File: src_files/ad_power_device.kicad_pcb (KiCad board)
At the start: 2 copper layers, 75 x 75 mm, 508 parts, among them IC1 TPS62867RQYR, IC2 TPS61288RQQR, J1 SPEAKER, J10 Conn_01x02_Male, J11 USB_C_Receptacle, J12 DEBUG_4G, J13 U.FL-R-SMT-1(10), J14 U.FL-R-SMT-1(10), J15 U.FL-R-SMT-1(10), J16 U.FL-R-SMT-1(10), J2 5622-6309-ML, J3 205957-0271, J4 2001-1-2-21-00-BK, J5 3-1734592-0, J6 3-1734592-0, J7 Conn_01x05_Male, J8 2001-1-2-21-00-BK, J9 SIM_Card, Q1 DTC143ZEBTL, Q10 DTC143ZEBTL, Q11 IRFR9024NTRPBF, Q2 DTC143ZEBTL, Q3 2SK3018, Q4 2SK3018, Q5 2SK3018, Q6 DTC143ZEBTL, Q7 DTC143ZEBTL, Q8 DTC143ZEBTL, Q9 DTC143ZEBTL, SW1 PWR_ON, SW2 RESET BTN, SW3 RECOVER BTN, U1 RK3566, U10 ESD5304D-TP, U11 NFC_VS1797SM, U12 MCDP2900, U13 ZLDO1117G12TA, U14 ESD5304D-TP, U15 ESD5304D-TP, U16 ESD5304D-TP, U17 SY6280AAAC, U18 ESD5304D-TP, U19 quesctel_EG91-EX, U2 RK809, U20 ESD5304D-TP, U21 SY6912A, U3 AP6256, U4 LPDDRS_32_IS43LQ32128A-062BLI, U5 TLV62569PDDCR, U6 TLV62569PDDCR, U7 QUECTEL_L70-RL, U8 ESD5304D-TP, U9 ESD5304D-TP, Y1 32.768KHz, Y2 37.4MHz_10PPM, Y3 24MHz/10ppm, Y4 27MHz

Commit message: updated footprint and schematics
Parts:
- removed D2: LED, LED_SMD:LED_0201_0603Metric_Pad0.64x0.40mm_HandSolder
- removed J10: Conn_01x02_Male, Connector_Phoenix_MC:PhoenixContact_MC_1,5_2-G-3.81_1x02_P3.81mm_Horizontal
- removed J12: DEBUG_4G, Connector_PinHeader_2.54mm:PinHeader_1x02_P2.54mm_Vertical
- removed J15: U.FL-R-SMT-1(10), greencharge-footprints:HRS_U.FL-R-SMT-1(10)
- removed Q1, Q2: DTC143ZEBTL, greencharge-footprints:SOTFL50P160X85-3N
- added C284: 10nF, Capacitor_SMD:C_0402_1005Metric, B.Cu at (23.0, 180.8)
- added C285: 10nF, Capacitor_SMD:C_0402_1005Metric, B.Cu at (31.2, 159.4)
- added D26: SMF11A, Diode_SMD:D_SOD-123, B.Cu at (32.6, 166.0)
- added D27: LED_GREEN, LED_SMD:LED_0603_1608Metric, B.Cu at (37.5, 166.4)
- added JP1: Jumper, TestPoint:TestPoint_2Pads_Pitch2.54mm_Drill0.8mm, F.Cu at (24.2, 212.7)
- added Q12: DTC143ZEBTL, greencharge-footprints:SOTFL50P160X85-3N, B.Cu at (25.2, 180.7)
- added R106: 4.7K, Resistor_SMD:R_0402_1005Metric, B.Cu at (34.1, 161.4)
- added R107: 4.7K, Resistor_SMD:R_0402_1005Metric, B.Cu at (31.2, 161.4)
- added R108: 4.7K, Resistor_SMD:R_0402_1005Metric, B.Cu at (34.1, 163.4)
- added R109: 0R, Resistor_SMD:R_0402_1005Metric, B.Cu at (27.6, 181.5)
- added TP18: PWR_IN+, TestPoint:TestPoint_Pad_2.0x2.0mm, B.Cu at (14.7, 205.9)
- added TP19: PWR_IN-, TestPoint:TestPoint_Pad_2.0x2.0mm, B.Cu at (14.7, 210.0)
- added TP20: DBG_RXD, TestPoint:TestPoint_Pad_2.0x2.0mm, F.Cu at (19.3, 150.6)
- added TP21: DBG_RXD, TestPoint:TestPoint_Pad_2.0x2.0mm, F.Cu at (19.9, 145.8)
- C103, C106, C131, C228, C260, C261, C262, C263, C264, C265, C266, C267, C270, C271, C272, C273, C274, C275, C276, C277, C278, C279, C280, C281, C282, C78, C80, C81, C82, D13, D15, IC2, J13, J14, J16, J3, L11, Q10, Q3, Q4, Q5, Q6, R100, R101, R102, R103, R104, R105, R26, R27, R71, R81, TP12, TP13, TP14, TP15, U6: moved to B.Cu
- C149: value 10uF -> 22uF; moved to F.Cu
- C150: value 100nF -> 22uF; moved to F.Cu
- C226, C230: footprint Capacitor_SMD:CP_Elec_5x5.4 -> Capacitor_Tantalum_SMD:CP_EIA-3216-18_Kemet-A
- C251: value 130pF -> 3200pF
- C283: value 100nF -> 22uF
- D1: value LED -> SS56; footprint LED_SMD:LED_0201_0603Metric_Pad0.64x0.40mm_HandSolder -> greencharge-footprints:SMAG; moved to B.Cu
- D20: value LED -> LED_GREEN
- J4: value 2001-1-2-21-00-BK -> 3-1734592-0; footprint digikey-footprints:HDMI_Mini_Female_2001-1-2-21-00-BK -> greencharge-footprints:TE_3-1734592-0
- J8: value 2001-1-2-21-00-BK -> 3-1734592-0; footprint digikey-footprints:HDMI_Mini_Female_2001-1-2-21-00-BK -> greencharge-footprints:TE_3-1734592-0; moved to B.Cu
- J9: value SIM_Card -> SIM_Card_Shielded; footprint greencharge-footprints:MOLEX_78800-0001 -> greencharge-footprints:GCT_SIM8066-6-1-14-01-A_REVA
- R28: value 0R -> 100K
- R29: value 1K -> 806K
- R30: value 1K -> 91K
- U1: footprint greencharge-footprints:BGA828C65P31X31_2100X2100X161N -> greencharge-footprints:RK366_BGA-565_20x18_15.5x14.4mm
- U13: moved to F.Cu
- U19: value quesctel_EG91-EX -> EG25G; footprint greencharge-footprints:XCVR_EG91EFB-512-SNND -> greencharge-footprints:XCVR_EG25G
- U4: value LPDDRS_32_IS43LQ32128A-062BLI -> LPDDR4_32_IS43LQ32128A-062BLI
- U7: value QUECTEL_L70-RL -> TPS63802DLAR; footprint greencharge-footprints:QUECTEL_L70-R -> greencharge-footprints:VREG_TPS63802DLAR; moved to B.Cu
- moved R104 114.5 mm to (53.3, 217.8)
- moved U6 111.9 mm to (49.4, 216.5)
- moved R103 110.6 mm to (53.3, 215.8)
- moved IC2 110.5 mm to (43.7, 215.8)
- moved C271 106.6 mm to (54.4, 213.8)
- moved R101 106.0 mm to (51.3, 213.9)
- moved C283 95.9 mm to (83.7, 197.4)
- moved R28 94.9 mm to (83.4, 195.7)
- moved TP13 90.1 mm to (41.3, 199.0)
- moved C273 85.0 mm to (43.2, 196.5)
- moved R100 85.0 mm to (40.3, 196.5)
- moved R26 83.4 mm to (83.8, 211.6), turned to 90 degrees
- moved C103 82.3 mm to (85.9, 211.0)
- moved C265 82.0 mm to (85.8, 212.4)
- moved C267 81.8 mm to (82.5, 211.8), turned to 90 degrees
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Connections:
- C149 pad 1: +3V3 -> VBAT
- C150 pad 1: +3V3 -> Net-(C150-Pad1)
- C234 pad 1: /4G_MODULE/USM1_DATA -> Net-(C234-Pad1)
- C283 pad 1: +3V3 -> Net-(C150-Pad1)
- D1 pad 1: Net-(D1-Pad1) -> +5V
- D1 pad 2: +3V3 -> Net-(C150-Pad1)
- J2 pad S2: (no net) -> /SATA1_TX+
- J4 pad 1: /RK3566_PART_C/HDMI_TX2P_PORT+ -> (no net)
- J4 pad 10: /RK3566_PART_C/HDMI_TXCLKP_PORT+ -> (no net)
- J4 pad 11: GND -> (no net)
- J4 pad 12: /RK3566_PART_C/HDMI_TXCLKN_PORT- -> (no net)
- J4 pad 13: /RK3566_PART_C/HDMI_TX_CEC_PORT -> (no net)
- J4 pad 15: /RK3566_PART_C/HDMI_TXDDC_SCL_PORT -> (no net)
- J4 pad 16: /RK3566_PART_C/HDMI_TXDDC_SDA_PORT -> (no net)
- J4 pad 17: GND -> (no net)
- J4 pad 18: /RK3566_PART_C/VCC5V_HDMI_TX -> (no net)
- J4 pad 19: /RK3566_PART_C/HDMI_TX_HPD_PORT -> (no net)
- J4 pad 2: GND -> (no net)
- J4 pad 3: /RK3566_PART_C/HDMI_TX2N_PORT- -> (no net)
- J4 pad 4: /RK3566_PART_C/HDMI_TX1P_PORT+ -> (no net)
- J4 pad 5: GND -> (no net)
- J4 pad 6: /RK3566_PART_C/HDMI_TX1N_PORT- -> (no net)
- J4 pad 7: /RK3566_PART_C/HDMI_TX0P_PORT+ -> (no net)
- J4 pad 8: GND -> (no net)
- J4 pad 9: /RK3566_PART_C/HDMI_TX0N_PORT- -> (no net)
- J5 pad 10: (no net) -> /TP_INT_GPIO0_A5
- J5 pad 13: (no net) -> /LCD_RST_L_GPIO0_C2
- J5 pad 16: (no net) -> /RK3566_PART_C/MIPI_DSI_TX0_D0P+
- J5 pad 17: (no net) -> /RK3566_PART_C/MIPI_DSI_TX0_D0N-
- J5 pad 19: (no net) -> /RK3566_PART_C/MIPI_DSI_TX0_D1P+
- J5 pad 20: (no net) -> /RK3566_PART_C/MIPI_DSI_TX0_D1N-
- J5 pad 25: (no net) -> /RK3566_PART_C/MIPI_DSI_TX0_D2P+
- J5 pad 26: (no net) -> /RK3566_PART_C/MIPI_DSI_TX0_D2N-
- J5 pad 29: (no net) -> /RK3566_PART_C/MIPI_DSI_TX0_D3N-
- J6 pad 10: (no net) -> /TP_INT_GPIO1_B6_DISPLAY_ONE
- J6 pad 12: (no net) -> /RK3566_PART_C/LCD_BL_PWM12_M0_DISPLAY_ONE
- J6 pad 13: (no net) -> /LCD_RST_L_GPIO1_C0_DISPLAY_ONE
- J6 pad 16: (no net) -> /RK3566_PART_C/MIPI_DSI_TX1_D0P+
- J6 pad 17: (no net) -> /RK3566_PART_C/MIPI_DSI_TX1_D0N-
- J6 pad 20: (no net) -> /RK3566_PART_C/MIPI_DSI_TX1_D1N-
- J6 pad 25: (no net) -> /RK3566_PART_C/MIPI_DSI_TX1_D2P+
- J6 pad 26: (no net) -> /RK3566_PART_C/MIPI_DSI_TX1_D2N-
- J6 pad 29: (no net) -> /RK3566_PART_C/MIPI_DSI_TX1_D3N-
- J6 pad 5: (no net) -> /GPIO1_B4_DISPLAY_ONE
- J8 pad 1: /RK3566_PART_C/DP TO HDMI/TMDS_D2+ -> (no net)
- J8 pad 10: /RK3566_PART_C/DP TO HDMI/TMDS_CLK+ -> (no net)
- J8 pad 11: GND -> (no net)
- J8 pad 12: /RK3566_PART_C/DP TO HDMI/TMDS_CLK- -> (no net)
- J8 pad 13: /RK3566_PART_C/DP TO HDMI/CEC -> (no net)
- J8 pad 15: /RK3566_PART_C/DP TO HDMI/DDC_CLK -> (no net)
- J8 pad 16: /RK3566_PART_C/DP TO HDMI/DDC_DATA -> (no net)
- J8 pad 17: GND -> (no net)
- J8 pad 18: /RK3566_PART_C/DP TO HDMI/VCC5V_HDMI_TX -> (no net)
- J8 pad 19: /RK3566_PART_C/DP TO HDMI/HPD -> (no net)
- J8 pad 2: GND -> (no net)
- J8 pad 3: /RK3566_PART_C/DP TO HDMI/TMDS_D2- -> (no net)
- J8 pad 4: /RK3566_PART_C/DP TO HDMI/TMDS_D1+ -> (no net)
- J8 pad 5: GND -> (no net)
- J8 pad 6: /RK3566_PART_C/DP TO HDMI/TMDS_D1- -> (no net)
- J8 pad 7: /RK3566_PART_C/DP TO HDMI/TMDS_D0+ -> (no net)
- J8 pad 8: GND -> (no net)
- J8 pad 9: /RK3566_PART_C/DP TO HDMI/TMDS_D0- -> (no net)
- Q10 pad 1: Net-(Q10-Pad1) -> /4G_MODULE/Status_indicator
- Q8 pad 1: (no net) -> /4G_MODEM_ON
- Q8 pad 3: Net-(Q8-Pad3) -> /4G_MODULE/PWR_EN
- Q9 pad 1: (no net) -> /4G_MODEM_RESETn
- Q9 pad 3: Net-(Q9-Pad3) -> /4G_MODULE/RESET_n
- R17 pad 1: (no net) -> /I2S2_SCLK_TX_M0
- R18 pad 1: (no net) -> /I2S2_SDI_M0
- R28 pad 1: Net-(J15-Pad2) -> Net-(C150-Pad1)
- R29 pad 1: Net-(D1-Pad1) -> Net-(C150-Pad1)
- R29 pad 2: Net-(Q1-Pad3) -> /BATTERY_CHARGER/FB
- R30 pad 1: Net-(D2-Pad1) -> /BATTERY_CHARGER/FB
- R30 pad 2: Net-(Q2-Pad3) -> GND
- R37 pad 1: (no net) -> Net-(R37-Pad1)
- R38 pad 1: (no net) -> Net-(R38-Pad1)
- R40 pad 1: (no net) -> Net-(R40-Pad1)
- R41 pad 1: (no net) -> Net-(R41-Pad1)
- R41 pad 2: /RK3566_PART_C/HDMI_TX0P_PORT+ -> (no net)
- R42 pad 1: (no net) -> Net-(R42-Pad1)
- R43 pad 1: (no net) -> Net-(R43-Pad1)
- R44 pad 1: (no net) -> Net-(R44-Pad1)
- R48 pad 2: (no net) -> /RK3566_LPDDR3/I2C1_SCL
- R49 pad 2: (no net) -> /RK3566_LPDDR3/I2C1_SDA
- R79 pad 2: Net-(R79-Pad2) -> /4G_MODULE/ANT_GNSS_GPS
- R80 pad 2: Net-(R80-Pad2) -> /4G_MODULE/ANT_MAIN
- R81 pad 1: /4G_MODULE/USM1_DATA -> Net-(C234-Pad1)
- TP9 pad 1: (no net) -> Net-(TP9-Pad1)
- U1 pad V1: (no net) -> Net-(U1-PadV1)
- U1 pad V2: (no net) -> Net-(U1-PadV2)
- U12 pad A3: (no net) -> /RK3566_PART_C/EDP_TX_D2-
- U12 pad A4: (no net) -> /RK3566_PART_C/EDP_TX_D2+
- U12 pad A5: (no net) -> /RK3566_PART_C/EDP_TX_D1-
- U12 pad A6: (no net) -> /RK3566_PART_C/EDP_TX_D1+
- U12 pad A8: (no net) -> /RK3566_PART_C/EDP_TX_D0+
- U12 pad F6: (no net) -> /RK3566_PART_C/MCDP_I2C_SCL
- U19 pad 10: /4G_MODULE_USB_D- -> /4G_MODULE/USM_GND
- U19 pad 11: (no net) -> /4G_MODULE/DBG_RXD
- U19 pad 12: (no net) -> /4G_MODULE/DBG_TXD
- U19 pad 14: (no net) -> /4G_MODULE/USM1_VDD
- U19 pad 15: Net-(Q8-Pad3) -> /4G_MODULE/USM1_DATA
- U19 pad 16: (no net) -> /4G_MODULE/USM1_CLK
- U19 pad 17: Net-(Q9-Pad3) -> /4G_MODULE/USM1_RST
- U19 pad 18: (no net) -> Net-(U19-Pad113)
- U19 pad 19: (no net) -> GND
- U19 pad 2: (no net) -> /AP_READY
- U19 pad 20: (no net) -> /4G_MODULE/RESET_n
- U19 pad 21: Net-(Q10-Pad1) -> /4G_MODULE/PWR_EN
- U19 pad 22: Net-(J12-Pad2) -> GND
- U19 pad 23: Net-(J12-Pad1) -> (no net)
- U19 pad 3: GND -> Net-(U19-Pad113)
- U19 pad 31: GND -> (no net)
- U19 pad 32: VCC_3V3 -> (no net)
- U19 pad 33: VCC_3V3 -> (no net)
- U19 pad 36: (no net) -> GND
- U19 pad 41: (no net) -> /4G_MODULE_SDA
- U19 pad 42: (no net) -> /4G_MODULE_SCL
- U19 pad 43: /4G_MODULE/USM1_VDD -> Net-(U19-Pad113)
- U19 pad 44: /4G_MODULE/USM1_RST -> (no net)
- U19 pad 45: /4G_MODULE/USM1_DATA -> (no net)
- U19 pad 46: /4G_MODULE/USM1_CLK -> GND
- U19 pad 47: /4G_MODULE/USM_GND -> /4G_MODULE/ANT_GNSS_GPS
- U19 pad 49: (no net) -> /4G_MODULE/ANT_MAIN
- U19 pad 51: (no net) -> GND
- U19 pad 52: VCC_3V3 -> GND
- U19 pad 53: VCC_3V3 -> GND
- U19 pad 55: GND -> Net-(U19-Pad113)
- U19 pad 56: Net-(R79-Pad2) -> GND
- U19 pad 57: (no net) -> VCC_3V3
- U19 pad 58: GND -> VCC_3V3
- U19 pad 59: GND -> VCC_3V3
- U19 pad 6: (no net) -> /4G_MODULE/Net_status
- U19 pad 60: Net-(R80-Pad2) -> VCC_3V3
- U19 pad 61: GND -> /4G_MODULE/Status_indicator
- U19 pad 62: GND -> (no net)
- U19 pad 67: GND -> (no net)
- U19 pad 68: GND -> (no net)
- U19 pad 69: GND -> /4G_MODULE_USB_D+
- U19 pad 7: (no net) -> /4G_MODULE/1.8V_local_ldo
- U19 pad 70: GND -> /4G_MODULE_USB_D-
- U19 pad 71: GND -> VCC_3V3
- U19 pad 8: VCC_3V3 -> GND
- U19 pad 85: (no net) -> GND
- U19 pad 86: (no net) -> GND
- U19 pad 87: (no net) -> GND
- U19 pad 88: (no net) -> GND
- U19 pad 9: /4G_MODULE_USB_D+ -> GND
- U19 pad 92: (no net) -> GND
- U19 pad 93: (no net) -> GND
- U19 pad 94: (no net) -> GND
- U19 pad 95: (no net) -> GND
- U19 pad 96: (no net) -> GND
- U19 pad 97: (no net) -> GND
- U19 pad 98: (no net) -> GND
- U19 pad 99: (no net) -> GND
- U2 pad 16: /I2S1_MCLK_M0_RK809 -> (no net)
- U3 pad 13: (no net) -> /WIFI_WAKE_HOST_H_GPIO2_B2
- U3 pad 16: (no net) -> /SDMMC1_CLK
- U3 pad 17: (no net) -> /SDMMC1_CMD
- U3 pad 37: (no net) -> /BT_WAKE_HOST_H_GPIO2_C0
- U3 pad 41: (no net) -> /UART1_CTSn_M0
- U3 pad 42: (no net) -> /UART1_TX_M0
- U3 pad 44: (no net) -> /UART1_RTSn_M0
- U7 pad 1: GND -> VBAT
- U7 pad 10: GND -> VBAT
- U7 pad 2: (no net) -> GND
- U7 pad 3: (no net) -> GND
- U7 pad 4: /IPPS -> /BATTERY_CHARGER/FB
- U7 pad 5: /STANDBY -> Net-(R28-Pad2)
- U7 pad 6: (no net) -> Net-(C150-Pad1)
- U7 pad 8: +3V3 -> GND
- U7 pad 9: +3V3 -> (no net)
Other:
- board text added: "4G_MODULE + GPS MODULE"
- board text added: "5G_RADAR_MODULE"
- board text added: "ANTENNA"
- board text added: "AP6256_WIFI/BT"
- board text added: "AUDIO_OUT"
- board text added: "BAT_CHARGER_IC"
- board text added: "HDMI_MINI"
- board text added: "MIPI_CON_1"
- board text added: "MIPI_CON_2"
- board text added: "MIPI_CON_3"
- board text added: "MIPI_CON_4"
- board text added: "NANO_SIM_CON"
- board text added: "NFC_READER"
- board text added: "RAM_LPDDR4_4GB"
- board text added: "RK3566_MAIN_IC"
- board text added: "RK809_PMIC"
- board text added: "SATA_CONNECTOR"
- board text added: "USB_PWR IN_OTG"
- board text added: "VS1797SM"

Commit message: complete update on schematiC + FOOTPRINT
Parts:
- removed D10, D4, D5: 1N5819WS, Diode_SMD:D_SOD-323
- removed D11, D6: ESD5451R-2/TR, greencharge-footprints:DFP1006-2L
- removed D7, D8, D9: D, Diode_SMD:D_SOD-123
- removed FB3, FB4: MPZ1608S471ATD25, Inductor_SMD:L_0603_1608Metric
- removed Q3, Q4, Q5: 2SK3018, digikey-footprints:SOT-23-3
- removed R66: 100K, Resistor_SMD:R_0805_2012Metric
- removed R67: 249OHM/1%, Resistor_SMD:R_0603_1608Metric
- removed R68, R69, R70: 4.7K, Resistor_SMD:R_0402_1005Metric
- removed U13: ZLDO1117G12TA, Package_TO_SOT_SMD:SOT-223-3_TabPin2
- removed U14, U15, U16: ESD5304D-TP, greencharge-footprints:ESD5304D-TP
- added C286: 100nF, Capacitor_SMD:C_0402_1005Metric, F.Cu at (22.6, 193.8)
- added C287: 100nF, Capacitor_SMD:C_0402_1005Metric, F.Cu at (56.7, 159.0)
- added C288: 100nF, Capacitor_SMD:C_0402_1005Metric, F.Cu at (59.6, 159.0)
- added C289: 100nF, Capacitor_SMD:C_0402_1005Metric, F.Cu at (81.4, 169.8)
- added C290: 100nF, Capacitor_SMD:C_0402_1005Metric, F.Cu at (81.1, 168.2)
- added C291: 100nF, Capacitor_SMD:C_0402_1005Metric, F.Cu at (39.0, 156.3)
- added C292: 100nF, Capacitor_SMD:C_0402_1005Metric, F.Cu at (59.6, 157.0)
- added C293: 100nF, Capacitor_SMD:C_0402_1005Metric, F.Cu at (69.9, 161.4)
- added C294: 100nF, Capacitor_SMD:C_0402_1005Metric, F.Cu at (81.0, 172.7)
- added C295: 1uF, Capacitor_SMD:C_0402_1005Metric, F.Cu at (80.9, 171.3)
- added C296: 1uF, Capacitor_SMD:C_0402_1005Metric, F.Cu at (62.4, 159.0)
- added C297: 100nF, Capacitor_SMD:C_0402_1005Metric, F.Cu at (27.2, 185.3)
- added D2: 1N5819WS, Diode_SMD:D_SOD-323, F.Cu at (31.6, 186.1)
- added L15: 470nH, greencharge-footprints:FNR4018SR47NT, B.Cu at (27.4, 203.7)
- added Y5: ASE-27.000MHZ-LR-T(27MHz), Crystal:Crystal_SMD_EuroQuartz_MT-4Pin_3.2x2.5mm, F.Cu at (35.9, 195.8)
- C176, C191, C203, C205: moved to F.Cu
- C190, C208: value 1uF -> 100nF; moved to F.Cu
- C192, C193, C196, C197, C199, C200, C201, C202: value 0.1uF -> 100nF; moved to F.Cu
- C194: value 22pF -> 100nF
- C195: value 22pF -> 100nF; moved to F.Cu
- C198: value 0.1uf -> 100nF; moved to F.Cu
- C204: value 2.2uF -> 10uF; footprint Capacitor_SMD:C_0402_1005Metric -> Capacitor_SMD:C_0603_1608Metric; moved to F.Cu
- C206: value 10uF -> 1uF; footprint Capacitor_SMD:C_0603_1608Metric -> Capacitor_SMD:C_0402_1005Metric
- C207: value 1uF -> 0.1uF; moved to F.Cu
- D3: value 1N5819WS -> ESD5451R-2/TR; footprint Diode_SMD:D_SOD-323 -> greencharge-footprints:DFP1006-2L
- J9: value SIM_Card_Shielded -> SIM8066-6-1-14-01-A_REVA
- R46: value 1K -> 2.2K_5%; moved to F.Cu
- R47: value 100K -> 2.2K_402; moved to F.Cu
- R60: value 10K -> 2.2K_5%
- R61: value 10K -> 2.2K_402; moved to F.Cu
- R62: value 27K -> 1K
- R63: value 1.8K -> 2.2K_402; moved to F.Cu
- R64: value 1.8K -> 1K; moved to F.Cu
- R65: value 2.2K_402 -> 1KK; moved to F.Cu
- U10: value ESD5304D-TP -> TC358860XBG; footprint greencharge-footprints:ESD5304D-TP -> greencharge-footprints:TC358860XBG
- U12: value MCDP2900 -> TLV71211DBVR; footprint greencharge-footprints:BGA-64_8x8_7.0x7.0mm_MCDP2900 -> Package_TO_SOT_SMD:SOT-23-5; moved to F.Cu
- U8: value ESD5304D-TP -> TC358779XBG; footprint greencharge-footprints:ESD5304D-TP -> greencharge-footprints:TC358779XBG
- U9: value ESD5304D-TP -> ZLDO1117G12TA; footprint greencharge-footprints:ESD5304D-TP -> Package_TO_SOT_SMD:SOT-223-3_TabPin2
- Y4: value 27MHz -> ASE-27.000MHZ-LR-T(27MHz); footprint Crystal:Crystal_SMD_2016-4Pin_2.0x1.6mm -> Crystal:Crystal_SMD_EuroQuartz_MT-4Pin_3.2x2.5mm
- moved C206 63.7 mm to (69.9, 159.4)
- moved R61 61.5 mm to (19.8, 186.7)
- moved C208 57.1 mm to (56.7, 157.0), turned to 0 degrees
- moved R64 52.8 mm to (26.6, 190.5)
- moved C195 51.4 mm to (62.5, 172.6), turned to 0 degrees
- moved R62 50.8 mm to (22.6, 191.8)
- moved R63 48.7 mm to (86.0, 169.2)
- moved R47 48.5 mm to (60.8, 170.6)
- moved C176 45.9 mm to (28.4, 186.6)
- moved C196 45.2 mm to (59.6, 175.1), turned to 0 degrees
- moved U12 45.1 mm to (65.9, 160.2), turned to 0 degrees
- moved C201 42.8 mm to (59.6, 173.1), turned to 0 degrees
- moved C202 41.8 mm to (56.7, 175.1), turned to 0 degrees
- moved C205 40.7 mm to (57.3, 170.8), turned to 0 degrees
- moved R60 40.6 mm to (29.5, 189.5)
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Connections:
- net /RK3566_PART_C/MIPI_DSI_TX1_D0N- renamed /RK3566_PART_C/MIPI_DSI_TX1_D0-
- net /RK3566_PART_C/MIPI_DSI_TX1_D0P+ renamed /RK3566_PART_C/MIPI_DSI_TX1_D0+
- net /RK3566_PART_C/MIPI_DSI_TX1_D1N- renamed /RK3566_PART_C/MIPI_DSI_TX1_D1-
- net /RK3566_PART_C/MIPI_DSI_TX1_D2N- renamed /RK3566_PART_C/MIPI_DSI_TX1_D2-
- net /RK3566_PART_C/MIPI_DSI_TX1_D2P+ renamed /RK3566_PART_C/MIPI_DSI_TX1_D2+
- net /RK3566_PART_C/MIPI_DSI_TX1_D3N- renamed /RK3566_PART_C/MIPI_DSI_TX1_D3-
- C176 pad 1: /RK3566_PART_C/VCC5V_HDMI_TX -> +3V3
- C190 pad 1: +5V -> VCC_3V3
- C191 pad 1: /RK3566_PART_C/DP TO HDMI/1.2v_FB -> Net-(C191-Pad1)
- C193 pad 1: Net-(C193-Pad1) -> +3V3
- C194 pad 1: /RK3566_PART_C/DP TO HDMI/1.2v_FB -> +1V2
- C194 pad 2: /RK3566_PART_C/DP TO HDMI/TCLK -> GND
- C195 pad 1: /RK3566_PART_C/DP TO HDMI/1.2v_FB -> +1V2
- C195 pad 2: /RK3566_PART_C/DP TO HDMI/XTAL -> GND
- C196 pad 1: +3V3 -> +1V2
- C198 pad 1: GND -> +3V3
- C198 pad 2: /RK3566_PART_C/DP TO HDMI/1.2v_FB -> GND
- C199 pad 1: Net-(C199-Pad1) -> +1V2
- C200 pad 1: Net-(C199-Pad1) -> +1V2
- C201 pad 1: /RK3566_PART_C/DP TO HDMI/1.2v_FB -> +1V2
- C202 pad 1: GND -> +1V2
- C202 pad 2: +1V2 -> GND
- C203 pad 1: /RK3566_PART_C/DP TO HDMI/1.2v_FB -> Net-(C203-Pad1)
- C204 pad 1: Net-(C204-Pad1) -> +3V3
- C205 pad 1: +3V3 -> +1V2
- C206 pad 1: +1V2 -> +3V3
- C207 pad 1: +5V -> Net-(C207-Pad1)
- C208 pad 1: /RK3566_PART_C/DP TO HDMI/VCC5V_HDMI_TX -> +1V1
- C236 pad 1: /4G_MODULE/USM_GND -> GND
- D3 pad 1: Net-(D3-Pad1) -> /RK3566_PART_C/VCC5V_HDMI_TX
- D3 pad 2: +5V -> GND
- J4 pad 1: (no net) -> +5V
- J4 pad 10: (no net) -> /TP_INT_GPIO0_A5_DISPLAY_TWO
- J4 pad 11: (no net) -> /BL_EN_GPIO0_C0_DISPLAY_TWO
- J4 pad 15: (no net) -> GND
- J4 pad 16: (no net) -> /RK3566_PART_C/MIPI_D0+
- J4 pad 17: (no net) -> /RK3566_PART_C/MIPI_D0-
- J4 pad 18: (no net) -> GND
- J4 pad 19: (no net) -> /RK3566_PART_C/MIPI_D1+
- J4 pad 2: (no net) -> +5V
- J4 pad 20: (no net) -> /RK3566_PART_C/MIPI_D1-
- J4 pad 21: (no net) -> GND
- J4 pad 22: (no net) -> /RK3566_PART_C/MIPI_C+
- J4 pad 23: (no net) -> /RK3566_PART_C/MIPI_C-
- J4 pad 24: (no net) -> GND
- J4 pad 25: (no net) -> /RK3566_PART_C/MIPI_D2+
- J4 pad 26: (no net) -> /RK3566_PART_C/MIPI_D2-
- J4 pad 27: (no net) -> GND
- J4 pad 28: (no net) -> /RK3566_PART_C/MIPI_D3+
- J4 pad 29: (no net) -> /RK3566_PART_C/MIPI_D3-
- J4 pad 3: (no net) -> +5V
- J4 pad 30: (no net) -> GND
- J4 pad 4: (no net) -> GND
- J4 pad 5: (no net) -> /GPIO1_C2_u_DISPLAY_TWO
- J4 pad 6: (no net) -> VCC3V3_EXT
- J4 pad 7: (no net) -> /I2C2_SDA_M0_TP
- J4 pad 8: (no net) -> /I2C2_SCL_M0_TP
- J4 pad S1: Net-(J4-PadS1) -> GND
- J4 pad S2: Net-(J4-PadS1) -> GND
- J8 pad 1: (no net) -> +5V
- J8 pad 10: (no net) -> /RK3566_PART_C/TP_INT_GPIO0_A5_DISPLAY_THREE
- J8 pad 11: (no net) -> /RK3566_PART_C/BL_EN_GPIO0_C0_DISPLAY_THREE
- J8 pad 15: (no net) -> GND
- J8 pad 16: (no net) -> /RK3566_PART_C/DP TO MIPI/DSIODP_MIPI_D0+
- J8 pad 17: (no net) -> /RK3566_PART_C/DP TO MIPI/DSIODM_MIPI_D0-
- J8 pad 18: (no net) -> GND
- J8 pad 19: (no net) -> /RK3566_PART_C/DP TO MIPI/DSIODP_MIPI_D1+
- J8 pad 2: (no net) -> +5V
- J8 pad 20: (no net) -> /RK3566_PART_C/DP TO MIPI/DSIODM_MIPI_D1-
- J8 pad 21: (no net) -> GND
- J8 pad 22: (no net) -> /RK3566_PART_C/DP TO MIPI/DSIODP_MIPI_C+
- J8 pad 23: (no net) -> /RK3566_PART_C/DP TO MIPI/DSIODM_MIPI_C-
- J8 pad 24: (no net) -> GND
- J8 pad 25: (no net) -> /RK3566_PART_C/DP TO MIPI/DSIODP_MIPI_D2+
- J8 pad 26: (no net) -> /RK3566_PART_C/DP TO MIPI/DSIODM_MIPI_D2-
- J8 pad 27: (no net) -> GND
- J8 pad 28: (no net) -> /RK3566_PART_C/DP TO MIPI/DSIODP_MIPI_D3+
- J8 pad 29: (no net) -> /RK3566_PART_C/DP TO MIPI/DSIODM_MIPI_D3-
- J8 pad 3: (no net) -> +5V
- J8 pad 30: (no net) -> GND
- J8 pad 4: (no net) -> GND
- J8 pad 5: (no net) -> /RK3566_PART_C/GPIO1_C2_u_DISPLAY_THREE
- J8 pad 6: (no net) -> VCC3V3_EXT
- J8 pad 7: (no net) -> /I2C2_SDA_M0_TP
- J8 pad 8: (no net) -> /I2C2_SCL_M0_TP
- J8 pad 9: (no net) -> /RK3566_PART_C/LCD_3_ENGPIO1_C3_u_TO_DISPLAY
- J8 pad S1: Net-(J8-PadS1) -> GND
- J8 pad S2: Net-(J8-PadS1) -> GND
- J9 pad C1: (no net) -> /4G_MODULE/USM1_VDD
- J9 pad C2: (no net) -> Net-(C237-Pad1)
- J9 pad C3: (no net) -> Net-(C235-Pad1)
- J9 pad C5: (no net) -> GND
- J9 pad C7: (no net) -> Net-(C234-Pad1)
- J9 pad CD: (no net) -> GND
- J9 pad G1: (no net) -> GND
- J9 pad G2: (no net) -> GND
- J9 pad G3: (no net) -> GND
- J9 pad G4: (no net) -> GND
- R41 pad 2: (no net) -> /RK3566_PART_C/HDMI_TX0P_PORT+
- R46 pad 1: /RK3566_PART_C/HDMI_TX_HPDIN -> VCC3V3_PMU
- R46 pad 2: /RK3566_PART_C/HDMI_TX_HPD_PORT -> /RK3566_PART_C/MCDP_I2C_SDA
- R47 pad 1: /RK3566_PART_C/HDMI_TX_HPD_PORT -> +3V3
- R47 pad 2: GND -> Net-(C191-Pad1)
- R60 pad 1: VCC_3V3 -> VCC3V3_PMU
- R60 pad 2: /HDMITX_SDA -> /RK3566_PART_C/MCDP_I2C_SCL
- R61 pad 1: VCC_3V3 -> +3V3
- R61 pad 2: /HDMITX_SCL -> Net-(C203-Pad1)
- R62 pad 1: VCC_3V3 -> +1V1
- R62 pad 2: /HDMITX_CEC_M0 -> Net-(R62-Pad2)
- R63 pad 1: Net-(D3-Pad1) -> +3V3
- R63 pad 2: /RK3566_PART_C/HDMI_TXDDC_SCL_PORT -> Net-(C207-Pad1)
- R64 pad 1: Net-(D4-Pad1) -> Net-(R64-Pad1)
- R64 pad 2: /RK3566_PART_C/HDMI_TXDDC_SDA_PORT -> /RK3566_PART_C/HDMI_TX_HPDIN
- R65 pad 1: +3V3 -> Net-(R64-Pad1)
- R65 pad 2: Net-(C193-Pad1) -> GND
- R71 pad 1: (no net) -> /RK3566_LPDDR3/UART2_TX_M0_DEBUG
- U1 pad A27: (no net) -> /TP_INT_GPIO0_A5_DISPLAY_TWO
- U1 pad A29: (no net) -> /BL_EN_GPIO0_C0_DISPLAY_TWO
- U1 pad AP3: (no net) -> /RK3566_PART_C/BL_EN_GPIO0_C0_DISPLAY_THREE
- U1 pad AP4: (no net) -> /RK3566_PART_C/TP_INT_GPIO0_A5_DISPLAY_THREE
- U1 pad AP9: (no net) -> /RK3566_PART_C/GPIO1_C2_u_DISPLAY_THREE
- U1 pad AR4: (no net) -> /RK3566_PART_C/LCD_3_ENGPIO1_C3_u_TO_DISPLAY
- U1 pad AR7: (no net) -> /RK3566_PART_C/INT_hdmi_to_mipi
- U1 pad B30: (no net) -> /GPIO1_C2_u_DISPLAY_TWO
- U1 pad N37: (no net) -> /RK3566_PART_C/EDP_TX_D3+
- U1 pad N38: (no net) -> /RK3566_PART_C/EDP_TX_D3-
- U19 pad 10: /4G_MODULE/USM_GND -> GND
- U2 pad 69: (no net) -> GND
- U7 pad 7: (no net) -> Net-(L15-Pad1)
- U7 pad 9: (no net) -> Net-(L15-Pad2)
- U9 pad 1: /RK3566_PART_C/HDMI_TX_CEC_PORT -> +3V3
- U9 pad 2: /RK3566_PART_C/HDMI_TXCLKN_PORT- -> GND
- U9 pad 3: /RK3566_PART_C/HDMI_TXCLKP_PORT+ -> +1V2
- Y4 pad 1: /RK3566_PART_C/DP TO HDMI/TCLK -> +3V3
- Y4 pad 2: (no net) -> GND
- Y4 pad 3: /RK3566_PART_C/DP TO HDMI/XTAL -> Net-(U8-PadJ7)
- Y4 pad 4: (no net) -> +3V3

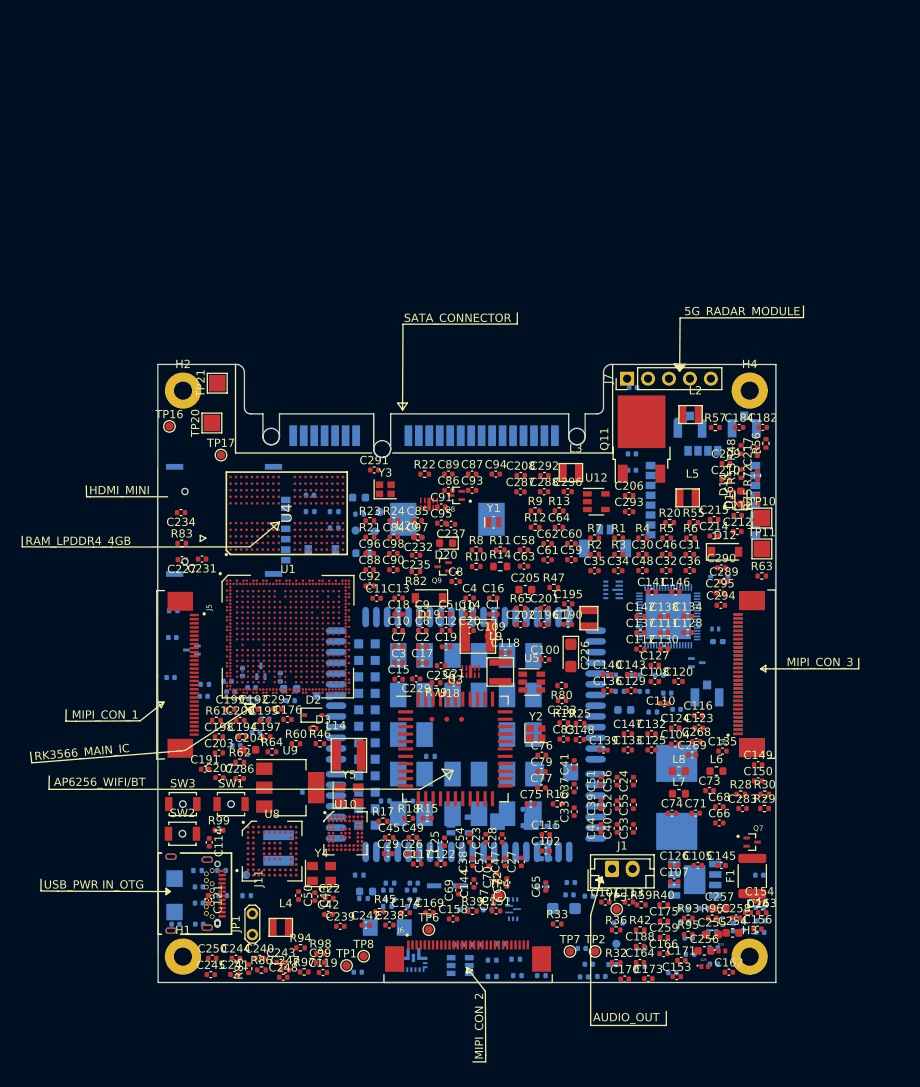
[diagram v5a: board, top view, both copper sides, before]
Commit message: wireless power TX RX added
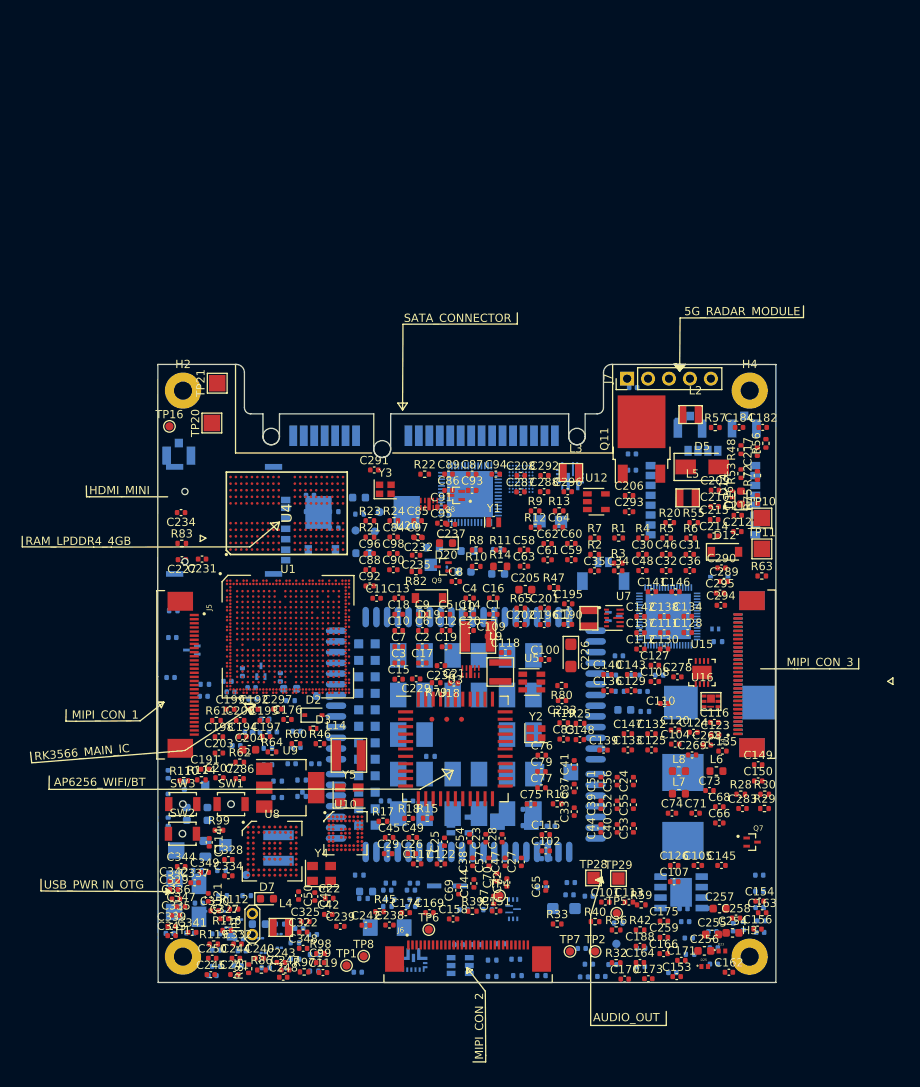
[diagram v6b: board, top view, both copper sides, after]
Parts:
- removed D24: ESD5451R-2/TR, greencharge-footprints:DFP1006-2L
- removed F1: mSMD300, Fuse:Fuse_1812_4532Metric
- removed J1: SPEAKER, Connector_JST:JST_EH_B2B-EH-A_1x02_P2.50mm_Vertical
- removed J11: USB_C_Receptacle, greencharge-footprints:GCT_USB4056-03-A_REVA
- added C298: 10uF, Capacitor_SMD:C_0402_1005Metric, B.Cu at (19.3, 217.7)
- added C299: 4.7nF, Capacitor_SMD:C_0402_1005Metric, B.Cu at (25.8, 216.7)
- added C300: 22nF, Capacitor_SMD:C_01005_0402Metric, B.Cu at (27.4, 214.3)
- added C301: 22nF, Capacitor_SMD:C_01005_0402Metric, B.Cu at (22.6, 210.9)
- added C302: 47nF, Capacitor_SMD:C_01005_0402Metric, B.Cu at (28.1, 216.9)
- added C303: 47nF, Capacitor_SMD:C_01005_0402Metric, B.Cu at (25.2, 213.1)
- added C304: 47nF, Capacitor_SMD:C_01005_0402Metric, B.Cu at (27.4, 212.6)
- added C305: 47nF, Capacitor_SMD:C_01005_0402Metric, B.Cu at (20.5, 209.9)
- added C306: 10uF, Capacitor_SMD:C_0402_1005Metric, B.Cu at (13.9, 193.2)
- added C307: 10uF, Capacitor_SMD:C_0402_1005Metric, B.Cu at (29.9, 211.9)
- added C308: 2.2uF, Capacitor_SMD:C_0603_1608Metric, B.Cu at (49.9, 168.7)
- added C309: 2.2uF, Capacitor_SMD:C_0603_1608Metric, B.Cu at (50.3, 166.2)
- added C310: 10uF, Capacitor_SMD:C_0603_1608Metric, B.Cu at (18.7, 198.1)
- added C311: 10uF, Capacitor_SMD:C_0603_1608Metric, B.Cu at (54.0, 168.9)
- added C312: 10uF, Capacitor_SMD:C_0603_1608Metric, B.Cu at (16.2, 198.1)
- added C313: 47nF, Capacitor_SMD:C_01005_0402Metric, B.Cu at (18.3, 209.9)
- added C314: 100nF, Capacitor_SMD:C_01005_0402Metric, B.Cu at (47.8, 168.3)
- added C315: 100nF, Capacitor_SMD:C_01005_0402Metric, B.Cu at (21.2, 211.9)
- added C316: 100nF, Capacitor_SMD:C_01005_0402Metric, B.Cu at (25.5, 214.9)
- added C317: 15uF, Capacitor_SMD:C_0805_2012Metric, B.Cu at (18.5, 202.3)
- added C318: 100nF, Capacitor_SMD:C_0402_1005Metric, B.Cu at (31.5, 212.7)
- added C319: 100nF, Capacitor_SMD:C_0402_1005Metric, B.Cu at (13.9, 196.1)
- added C320: 100pF, Capacitor_SMD:C_0402_1005Metric, B.Cu at (22.6, 213.2)
- added C322: 1uF, Capacitor_SMD:C_0402_1005Metric, F.Cu at (30.3, 212.4)
- added C323: 6.8nF, Capacitor_SMD:C_0402_1005Metric, B.Cu at (29.5, 190.0)
- added C324: 1uF, Capacitor_SMD:C_0402_1005Metric, B.Cu at (22.9, 214.7)
- added C325: 100nF, Capacitor_SMD:C_0402_1005Metric, F.Cu at (30.6, 211.1)
- added C326: 1uF, Capacitor_SMD:C_0402_1005Metric, B.Cu at (31.8, 192.0)
- added C327: 6.8nF, Capacitor_SMD:C_0402_1005Metric, F.Cu at (20.8, 210.8)
- added C328: 1uF, Capacitor_SMD:C_0402_1005Metric, F.Cu at (21.3, 203.6)
- added C329: 100nF, Capacitor_SMD:C_0402_1005Metric, F.Cu at (14.7, 207.2)
- added C330: 6.8nF, Capacitor_SMD:C_0402_1005Metric, B.Cu at (26.7, 188.1)
- added C331: 100nF, Capacitor_SMD:C_0402_1005Metric, B.Cu at (28.9, 192.0)
- added C332: 10uF, Capacitor_SMD:C_0402_1005Metric, F.Cu at (22.4, 213.8)
- added C333: 6.8nF, Capacitor_SMD:C_0402_1005Metric, B.Cu at (29.5, 188.0)
- added C334: 6.8nF, Capacitor_SMD:C_0402_1005Metric, F.Cu at (21.3, 205.6)
- added C335: 10uF, Capacitor_SMD:C_0402_1005Metric, F.Cu at (14.9, 210.4)
- added C336: 1nF, Capacitor_SMD:C_0402_1005Metric, F.Cu at (14.9, 208.4)
- added C337: 100nF_50V, Capacitor_SMD:C_0402_1005Metric, F.Cu at (17.2, 206.4)
- added C338: 100nF_50V, Capacitor_SMD:C_0402_1005Metric, B.Cu at (19.8, 212.6)
- added C339: 10uF, Capacitor_SMD:C_0402_1005Metric, F.Cu at (14.4, 211.7)
- added C340: 22nF_50V, Capacitor_SMD:C_0402_1005Metric, B.Cu at (19.8, 214.6)
- added C341: 22nF_50V, Capacitor_SMD:C_0402_1005Metric, F.Cu at (16.9, 212.4)
- added C342: 3.3nF, Capacitor_SMD:C_0402_1005Metric, F.Cu at (14.6, 206.2)
- added C343: 1nF, Capacitor_SMD:C_0402_1005Metric, F.Cu at (14.4, 212.8)
- added C344: 100nF, Capacitor_SMD:C_0402_1005Metric, F.Cu at (15.5, 204.4)
- added C345: 100nF, Capacitor_SMD:C_0402_1005Metric, B.Cu at (19.8, 216.5)
- added C346: 100nF, Capacitor_SMD:C_0402_1005Metric, B.Cu at (22.4, 216.4)
- added C347: 100nF, Capacitor_SMD:C_0402_1005Metric, F.Cu at (15.5, 209.3)
- added C348: 3.3nF, Capacitor_SMD:C_0402_1005Metric, F.Cu at (30.3, 214.4)
- added C349: 22nF_50V, Capacitor_SMD:C_0402_1005Metric, F.Cu at (18.4, 205.2)
- added C350: 3.3nF, Capacitor_SMD:C_0402_1005Metric, F.Cu at (19.6, 209.8)
- added D4: LED, LED_SMD:LED_0603_1608Metric, B.Cu at (25.0, 211.4)
- added D5: SMAJ16A, Diode_SMD:D_SMA, F.Cu at (78.8, 155.9)
- added D6: SMAJ16A, Diode_SMD:D_SMA, B.Cu at (17.7, 208.5)
- added D7: LED, LED_SMD:LED_0603_1608Metric, F.Cu at (25.9, 208.3)
- added D8: CDSU400B, Diode_SMD:D_0603_1608Metric, B.Cu at (46.1, 165.8)
- added IC3: P9038, Package_DFN_QFN:QFN-56-1EP_7x7mm_P0.4mm_EP5.6x5.6mm, B.Cu at (50.6, 159.2)
- added L16: MWSA1004S-3R3MT, greencharge-footprints:MWSA1004S-3R3MT, B.Cu at (76.2, 184.6)
- added R110: 10M, Resistor_SMD:R_0402_1005Metric, F.Cu at (15.8, 194.0)
- added R111: 10K, Resistor_SMD:R_0402_1005Metric, B.Cu at (27.2, 196.1)
- added R112: 10M, Resistor_SMD:R_0402_1005Metric, F.Cu at (21.9, 209.6)
- added R113: 4.7K, Resistor_SMD:R_0402_1005Metric, B.Cu at (27.2, 194.1)
- added R114: 4.7K, Resistor_SMD:R_0402_1005Metric, F.Cu at (18.0, 193.9)
- added R115: 4.7K, Resistor_SMD:R_0402_1005Metric, B.Cu at (30.2, 195.9)
- added R116: 0.01R, Resistor_SMD:R_0402_1005Metric, F.Cu at (21.1, 212.2)
- added R117: 10M, Resistor_SMD:R_0402_1005Metric, B.Cu at (30.2, 193.9)
- added R118: 10K, Resistor_SMD:R_0402_1005Metric, B.Cu at (26.1, 192.1)
- added R119: 47K, Resistor_SMD:R_0402_1005Metric, F.Cu at (19.5, 213.9)
- added R120: 1.5K, Resistor_SMD:R_0402_1005Metric, B.Cu at (23.8, 188.1)
- added R121: 15K, Resistor_SMD:R_0402_1005Metric, B.Cu at (26.1, 190.1)
- added R66: 470R, Resistor_SMD:R_0402_1005Metric, B.Cu at (31.7, 217.1)
- added R67: 470R, Resistor_SMD:R_0402_1005Metric, B.Cu at (53.9, 166.0)
- added R68: 47K, Resistor_SMD:R_0402_1005Metric, B.Cu at (29.3, 215.7)
- added R69: 47K, Resistor_SMD:R_0402_1005Metric, B.Cu at (14.0, 199.0)
- added R70: 47K, Resistor_SMD:R_0402_1005Metric, B.Cu at (14.4, 206.1)
- added TP22: RX_COIL+, TestPoint:TestPoint_Pad_1.5x1.5mm, B.Cu at (45.8, 167.8)
- added TP23: rx_vout, TestPoint:TestPoint_Pad_2.0x2.0mm, B.Cu at (14.9, 202.5)
- added TP24: USB_D-, TestPoint:TestPoint_Pad_1.0x1.0mm, B.Cu at (21.6, 212.9)
- added TP25: USB_D+, TestPoint:TestPoint_Pad_1.0x1.0mm, B.Cu at (18.4, 194.5)
- added TP26: TX_COIL-, TestPoint:TestPoint_Pad_1.5x1.5mm, B.Cu at (59.0, 162.6)
- added TP27: TX_COIL+, TestPoint:TestPoint_Pad_1.5x1.5mm, B.Cu at (61.6, 162.6)
- added TP28: SPK-, TestPoint:TestPoint_Pad_1.5x1.5mm, F.Cu at (65.6, 205.8)
- added TP29: SPK+, TestPoint:TestPoint_Pad_1.5x1.5mm, F.Cu at (68.6, 205.9)
- added U13: STWLC68, greencharge-footprints:STWLC68, B.Cu at (57.0, 157.5)
- added U14: TPS56637RPAR, greencharge-footprints:TPS56637RPAR, B.Cu at (62.7, 157.1)
- added U15: 24AA64T-I/OT, digikey-footprints:WFDFN-8-1EP_3x3mm, F.Cu at (78.7, 180.9)
- added U16: BRCS120N02ZJ, greencharge-footprints:BRCS120N02ZJ, F.Cu at (79.0, 183.8)
- C278, U7: moved to F.Cu
- R71: footprint Resistor_SMD:R_0402_1005Metric_Pad0.72x0.64mm_HandSolder -> Resistor_SMD:R_0402_1005Metric
- R93: value 5.1K -> 100K; moved to B.Cu
- R94: value 5.1K -> 20K; moved to B.Cu
- R95: value 2.2R -> 73.2K; moved to B.Cu
- R96: value 2.2R -> 10K; moved to B.Cu
- TP16: value VBUS -> 5V_VIN
- TP17: value 5V -> RX_COIL-; footprint TestPoint:TestPoint_Pad_D1.0mm -> TestPoint:TestPoint_Pad_1.5x1.5mm; moved to B.Cu
- moved J16 70.5 mm to (15.2, 154.6)
- moved R93 63.2 mm to (15.9, 194.6), turned to 90 degrees
- moved R96 48.5 mm to (31.7, 215.1)
- moved R95 47.7 mm to (29.3, 213.7)
- moved TP17 47.3 mm to (20.9, 201.8)
- moved Q6 11.5 mm to (68.0, 174.1)
- moved L11 10.3 mm to (37.5, 161.5)
- moved R40 8.56 mm to (65.8, 211.1)
- moved C281 7.40 mm to (68.7, 178.9)
- moved C120 5.91 mm to (75.5, 187.9)
- moved J3 3.97 mm to (66.8, 169.1)
- moved C278 3.94 mm to (75.8, 181.4)
- moved R94 3.80 mm to (27.5, 211.4)
- moved C209 3.51 mm to (80.3, 158.8)
- moved C210 3.51 mm to (80.3, 160.8)
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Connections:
- R93 pad 1: GND -> +5V
- R94 pad 1: GND -> +5V
- R95 pad 1: /USB_OTG0_D- -> +5V
- R95 pad 2: Net-(J11-PadA7) -> Net-(C320-Pad1)
- R96 pad 1: /USB_OTG0_D+ -> Net-(C320-Pad1)
- R96 pad 2: Net-(J11-PadA6) -> GND
- R97 pad 2: VBUS -> (no net)
- TP17 pad 1: +5V -> /USB)C_OTG_PWR_IN/COIL-
- TP18 pad 1: VBUS -> +5V
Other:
- board text added: "WIRELESS TX AND RX IC"
